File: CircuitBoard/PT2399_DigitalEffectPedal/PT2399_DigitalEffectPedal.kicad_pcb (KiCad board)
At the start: 4 copper layers, 75 x 78 mm, 126 parts, among them J1 POWER_SOURCE, J10 AudioInput_board, J12 AudioOutput_connector, J13 3PDT_AudioInput, J15 Encoder_connector, J16 Programming header, J17 Encoder_board_connector, J18 PUSH_STOMP, J2 SIG_OUTPUT_STOMP, J3 Power connector, J4 Battery_9V, J5 SIG_INPUT_STOMP, J6 POWER_INDICATOR, J7 AudioInput_board, J8 AudioInput_connector, J9 3PDT_AudioIOutput, Q1 BC547, Q2 BC547, U1 PT2399, U2 MCP6002-xSN, U3 MCP6002-xSN, U4 4066, U5 PT2399, U6 LM317_SOT-223, U7 AMS1117-5.0, U8 PIC16F72, Y1 Crystal

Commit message: PCB layout
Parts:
- removed J13: 3PDT_AudioInput, Connector_Pin:Pin_D1.0mm_L10.0mm
- removed J9: 3PDT_AudioIOutput, Connector_Pin:Pin_D1.0mm_L10.0mm
- added H1: MountingHole, MountingHole:MountingHole_3.2mm_M3, F.Cu at (105.0, 123.0)
- added H2: MountingHole, MountingHole:MountingHole_3.2mm_M3, F.Cu at (170.0, 122.9)
- added H3: MountingHole, MountingHole:MountingHole_3.2mm_M3, F.Cu at (105.0, 55.0)
- added H4: MountingHole, MountingHole:MountingHole_3.2mm_M3, F.Cu at (170.0, 55.0)
- J10: value AudioInput_board -> 3PDT_AudioIOutput; footprint Connector_PinHeader_2.54mm:PinHeader_1x06_P2.54mm_Vertical -> Connector_Pin:Pin_D1.0mm_L10.0mm
- J7: value AudioInput_board -> 3PDT_AudioInput; footprint Connector_PinHeader_2.54mm:PinHeader_1x06_P2.54mm_Vertical -> Connector_Pin:Pin_D1.0mm_L10.0mm
- moved J7 128.7 mm to (172.3, 79.5)
- moved J10 87.7 mm to (142.0, 67.3)
- moved RV1 77.2 mm to (103.0, 61.4), turned to 0 degrees
- moved D5 67.7 mm to (126.0, 56.4), turned to 180 degrees
- moved J6 67.5 mm to (115.5, 56.4)
- moved R31 67.5 mm to (119.5, 56.4)
- moved R26 63.8 mm to (139.6, 58.2), turned to 90 degrees
- moved R3 62.1 mm to (113.9, 66.0), turned to -90 degrees
- moved C9 59.1 mm to (117.2, 62.4), turned to -90 degrees
- moved R7 58.1 mm to (116.0, 66.0), turned to -90 degrees
- moved C35 57.7 mm to (144.9, 57.3), turned to 0 degrees
- moved C34 55.7 mm to (166.3, 65.1)
- moved C5 55.6 mm to (115.8, 71.1), turned to 0 degrees
- moved J4 55.5 mm to (158.6, 125.4), turned to -90 degrees
- moved R6 54.1 mm to (118.2, 66.0), turned to -90 degrees
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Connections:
- net Net-(J2-Pin_1) renamed SIG_OUT
- net Net-(J5-Pin_1) renamed SIG_IN
- J16 pad 1: +5V -> MCLR
- J16 pad 2: GNDA -> LED2_G
- J16 pad 3: LED2_G -> Net-(J16-Pin_3)
- J16 pad 4: Net-(J16-Pin_4) -> GNDA
- J16 pad 5: Net-(J16-Pin_5) -> +5V
- U8 pad 1: Net-(J16-Pin_5) -> MCLR
- U8 pad 28: Net-(J16-Pin_4) -> Net-(J16-Pin_3)
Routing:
- net Net-(R25-Pad1): track 0.00 -> 61.3 mm, vias 0 -> 3
- net +9V: track 0.00 -> 55.6 mm
- net Net-(Q1-C): track 0.00 -> 50.5 mm, vias 0 -> 2
- net Net-(R26-Pad1): track 0.00 -> 48.6 mm, vias 0 -> 2
- net PWM_B: track 0.00 -> 46.8 mm, vias 0 -> 2
- net Net-(U1-LPF2-OUT): track 0.00 -> 46.8 mm, vias 0 -> 2
- net CURR_B: track 0.00 -> 45.5 mm, vias 0 -> 2
- net CURR_A: track 0.00 -> 38.3 mm, vias 0 -> 2
- net +5V: track 0.00 -> 34.3 mm
- net ENC_B: track 0.00 -> 33.3 mm, vias 0 -> 2
- net Net-(J18-Pin_1): track 0.00 -> 32.4 mm
- net Net-(Q2-C): track 0.00 -> 31.0 mm
- net ENC_A: track 0.00 -> 29.8 mm, vias 0 -> 2
- net U4B: track 0.00 -> 25.6 mm
- net PWM_A: track 0.00 -> 25.6 mm
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- added copper zone on B.Cu, net GNDA
- added copper zone on F.Cu, net GNDA
- added copper zone on In2.Cu, net GNDA

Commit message: Layout PCB
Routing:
- net Net-(C6-Pad2): track 0.00 -> 57.7 mm, vias 0 -> 2
- net GNDA: track 9.86 -> 59.6 mm, vias 39 -> 48
- net Net-(U2A--): track 21.8 -> 65.0 mm, vias 2 -> 4
- net +5V: track 34.3 -> 55.0 mm, vias 0 -> 7
- net +4.5V: track 13.8 -> 23.6 mm, vias 0 -> 2
- net +9V: vias 0 -> 6
- added copper zone on F.Cu, net +5V
- added copper zone on In1.Cu, net +5V
- added copper zone on F.Cu, net +9V
- added copper zone on In1.Cu, net +9V

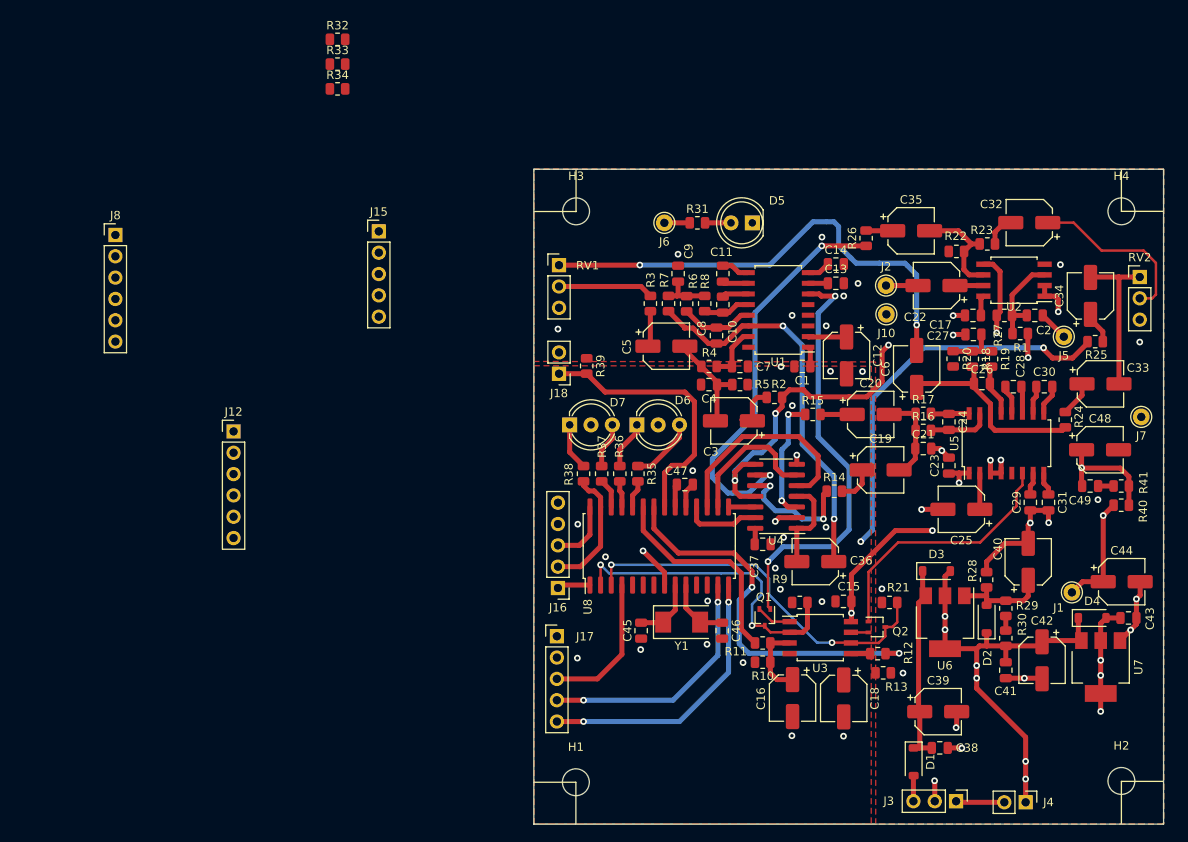
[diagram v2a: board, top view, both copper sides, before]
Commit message: PCB layout - main part
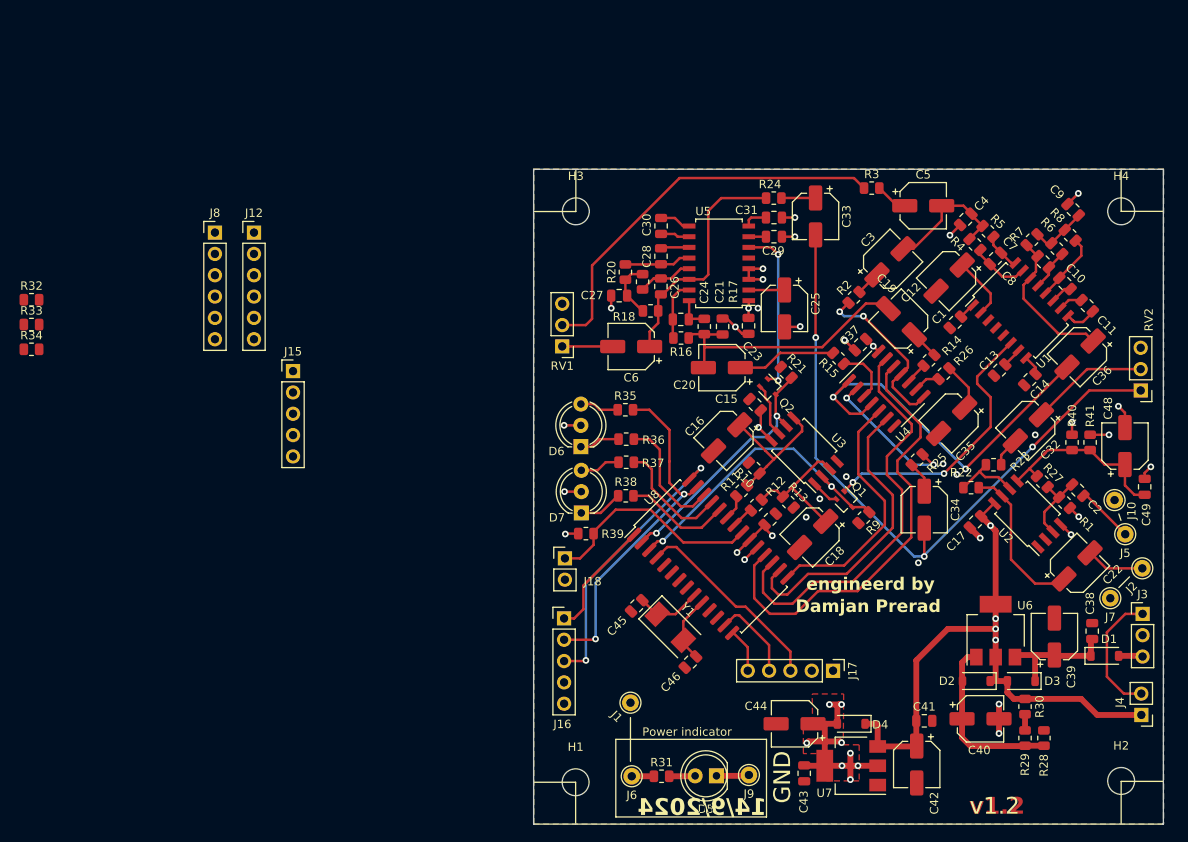
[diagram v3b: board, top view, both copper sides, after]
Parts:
- added J9: GND_POWER_INDICATOR, Connector_Pin:Pin_D1.0mm_L10.0mm, F.Cu at (125.6, 122.2)
- C47: value 22p -> 100n
- moved R31 66.1 mm to (115.2, 122.3)
- moved J6 66.0 mm to (111.7, 122.3)
- moved D5 66.0 mm to (121.8, 122.2)
- moved J1 54.2 mm to (111.5, 113.5)
- moved C30 49.5 mm to (115.2, 56.8), turned to -90 degrees
- moved R32 47.9 mm to (40.2, 65.5)
- moved R33 47.9 mm to (40.2, 68.5)
- moved R34 47.9 mm to (40.2, 71.4)
- moved C9 47.7 mm to (164.2, 54.8), turned to -45 degrees
- moved C31 47.1 mm to (128.6, 55.8), turned to 0 degrees
- moved J2 45.5 mm to (172.5, 97.5), turned to 0 degrees
- moved C28 44.8 mm to (115.1, 60.4), turned to -90 degrees
- moved R6 44.6 mm to (162.3, 59.5), turned to -45 degrees
- moved R8 44.3 mm to (163.9, 57.9), turned to -45 degrees
- moved C29 44.0 mm to (128.6, 58.0), turned to 0 degrees
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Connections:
- C16 pad 1: Net-(U3A-+) -> Net-(U3B-+)
- C18 pad 1: Net-(U3B-+) -> Net-(U3A-+)
- J16 pad 2: LED2_G -> LED1_R
- Q1 pad 3: CURR_A -> CURR_B
- Q2 pad 3: CURR_B -> CURR_A
- R10 pad 1: Net-(U3A-+) -> Net-(U3B-+)
- R11 pad 1: Net-(U3A-+) -> Net-(U3B-+)
- R12 pad 1: Net-(U3B-+) -> Net-(U3A-+)
- R13 pad 1: Net-(U3B-+) -> Net-(U3A-+)
- R21 pad 1: CURR_B -> CURR_A
- R9 pad 1: CURR_A -> CURR_B
- U3 pad 2: CURR_A -> CURR_B
- U3 pad 6: CURR_B -> CURR_A
- U8 pad 15: U4D -> U4B
- U8 pad 17: U4B -> U4A
- U8 pad 18: U4A -> U4D
- U8 pad 24: LED1_R -> LED2_G
- U8 pad 25: LED1_G -> LED2_R
- U8 pad 26: LED2_R -> LED1_G
- U8 pad 27: LED2_G -> LED1_R
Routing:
- net Net-(C33-Pad2): track 18.6 -> 81.8 mm, vias 0 -> 3
- net Net-(C6-Pad2): track 57.7 -> 6.02 mm, vias 2 -> 0
- net U4D: track 3.18 -> 53.1 mm
- net Net-(R26-Pad1): track 48.6 -> 3.15 mm, vias 2 -> 0
- net Net-(U2A--): track 65.0 -> 20.9 mm, vias 4 -> 2
- net PWM_B: track 46.8 -> 2.65 mm, vias 2 -> 0
- net Net-(R25-Pad1): track 61.3 -> 17.1 mm, vias 3 -> 2
- net U4A: track 9.11 -> 49.2 mm
- net LED1_R: track 3.31 -> 41.2 mm, vias 0 -> 2
- net Net-(R3-Pad1): track 11.3 -> 47.4 mm
- net Net-(C36-Pad2): track 11.9 -> 46.4 mm, vias 0 -> 2
- net Net-(U1-LPF2-OUT): track 46.8 -> 18.0 mm, vias 2 -> 0
- net ENC_B: track 33.3 -> 5.36 mm, vias 2 -> 0
- net Net-(J16-Pin_3): track 7.64 -> 33.2 mm, vias 0 -> 2
- net PWM_A: track 25.6 -> 2.96 mm
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- added copper zone on In2.Cu, net +5V
- added copper zone on In2.Cu, net +9V
- added copper zone on In1.Cu, net GNDA
- removed copper zone on In1.Cu, net +5V
- removed copper zone on F.Cu, net +9V
- removed copper zone on In1.Cu, net +9V
- removed copper zone on In2.Cu, net GNDA
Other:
- board text added: "+"
- board text added: "+5V"
- board text added: "12V"
- board text added: "14/9/2024"
- board text added: "Battery +9V"
- board text added: "Damjan Prerad"
- board text added: "ENC A"
- board text added: "ENC B"
- board text added: "GND"
- board text added: "LED"
- board text added: "MCLR"
- board text added: "PGC"
- board text added: "PGD"
- board text added: "POT"
- board text added: "POWER"
- board text added: "PUSH BUTTON"
- board text added: "Power indicator"
- board text added: "SIG IN"
- board text added: "SIG OUT"
- board text added: "engineerd by"
- board text added: "v1.2"

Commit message: Some warningss and errors fixed, added silk screen block diagram
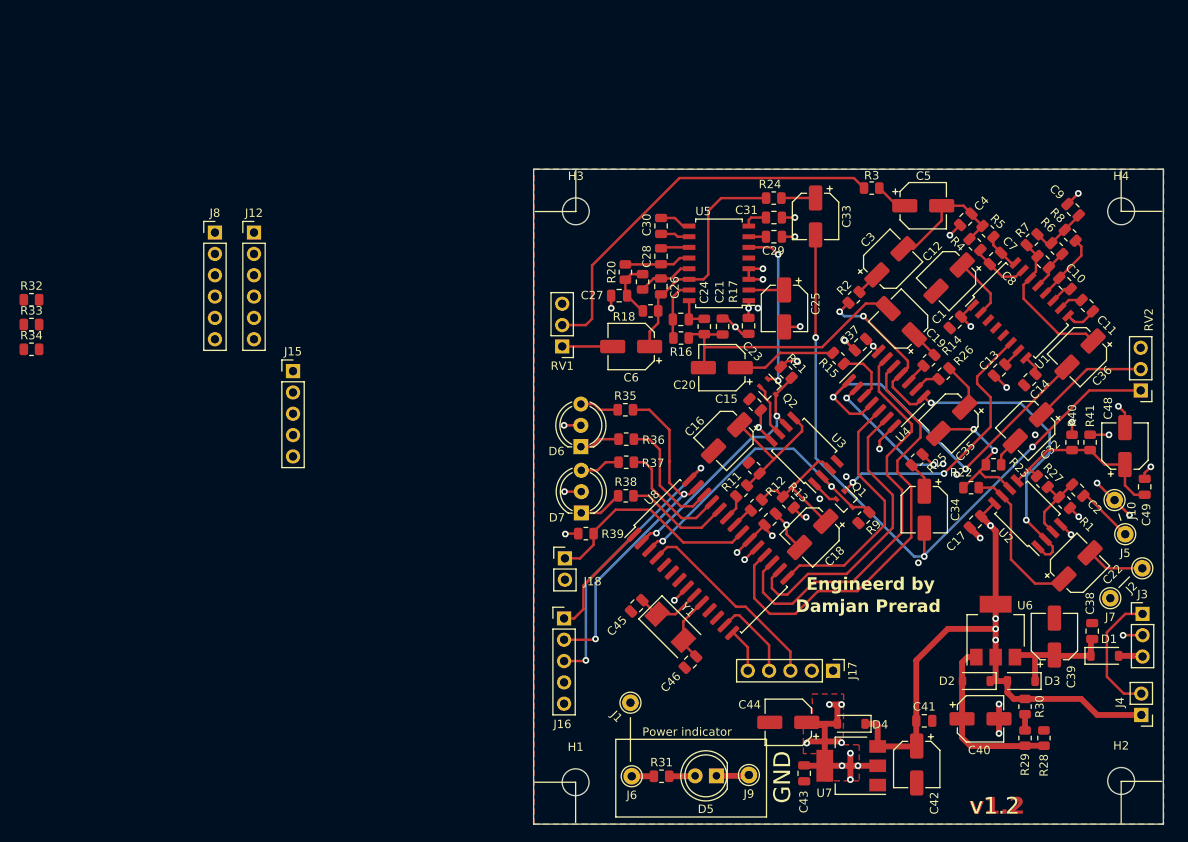
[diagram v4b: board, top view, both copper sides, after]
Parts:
- added  : LOGO, LOGO, B.Cu at (144.1, 60.7)
- moved C44 0.77 mm to (130.3, 115.9)
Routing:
- net Net-(U2A--): track 20.9 -> 56.6 mm, vias 2 -> 4
- net GNDA: track 41.7 -> 66.6 mm, vias 27 -> 35
- net Net-(U2B--): track 8.42 -> 18.5 mm, vias 0 -> 2
- net +5V: track 51.8 -> 55.8 mm, vias 17 -> 18
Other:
- board text added: "Delay/Echo/Reverb guitar pedal"
- board text added: "Engineerd by"
- board text added: "TIME MANIPULATOR"
- board text added: "The Time Manipulator is a programmable"
- board text removed: "engineerd by"

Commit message: Minor estetic changes to board layout
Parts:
-  : renamed from H4
-  : renamed from H3
-  : renamed from H2
-  : renamed from H1
-  : renamed from J1
- POWER IND: renamed from J6
- Push stomp: renamed from J18
- Tails pot: renamed from RV1
- Volume pot: renamed from RV2
- moved Power 5.04 mm to (172.4, 108.0), turned to 180 degrees
- renumbered J4 to Battery, J7 to GND, J10 to GND, J5 to IN, J2 to OUT, J16 to Porgramming, J3 to Power
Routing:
- net BAT_NEG: track 15.4 -> 4.47 mm
- net Net-(D1-A): track 2.88 -> 6.94 mm
- net GNDA: track 66.6 -> 64.3 mm, vias 35 -> 34
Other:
- board text added: "VOLUME POT"

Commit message: Minor estetic changes
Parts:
- moved   2.89 mm to (144.2, 63.6)
